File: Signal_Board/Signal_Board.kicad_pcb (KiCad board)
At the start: 2 copper layers, 54 x 43.5 mm, 17 parts, among them J1 Conn_01x02_Pin, J2 Conn_01x06_Pin, U1 74HC14, U2 LM317LZ, U3 4046

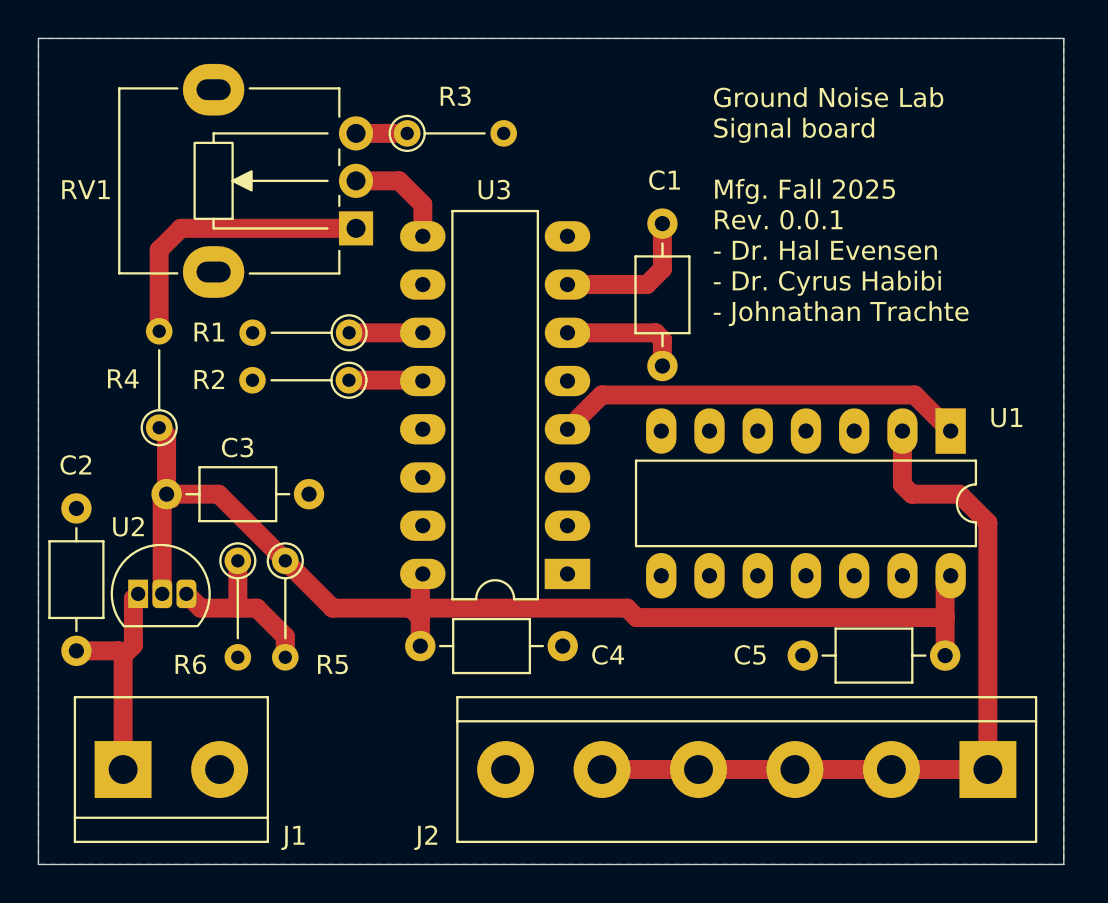
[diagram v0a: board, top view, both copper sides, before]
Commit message: Signal board version 0.0.2; updates in README
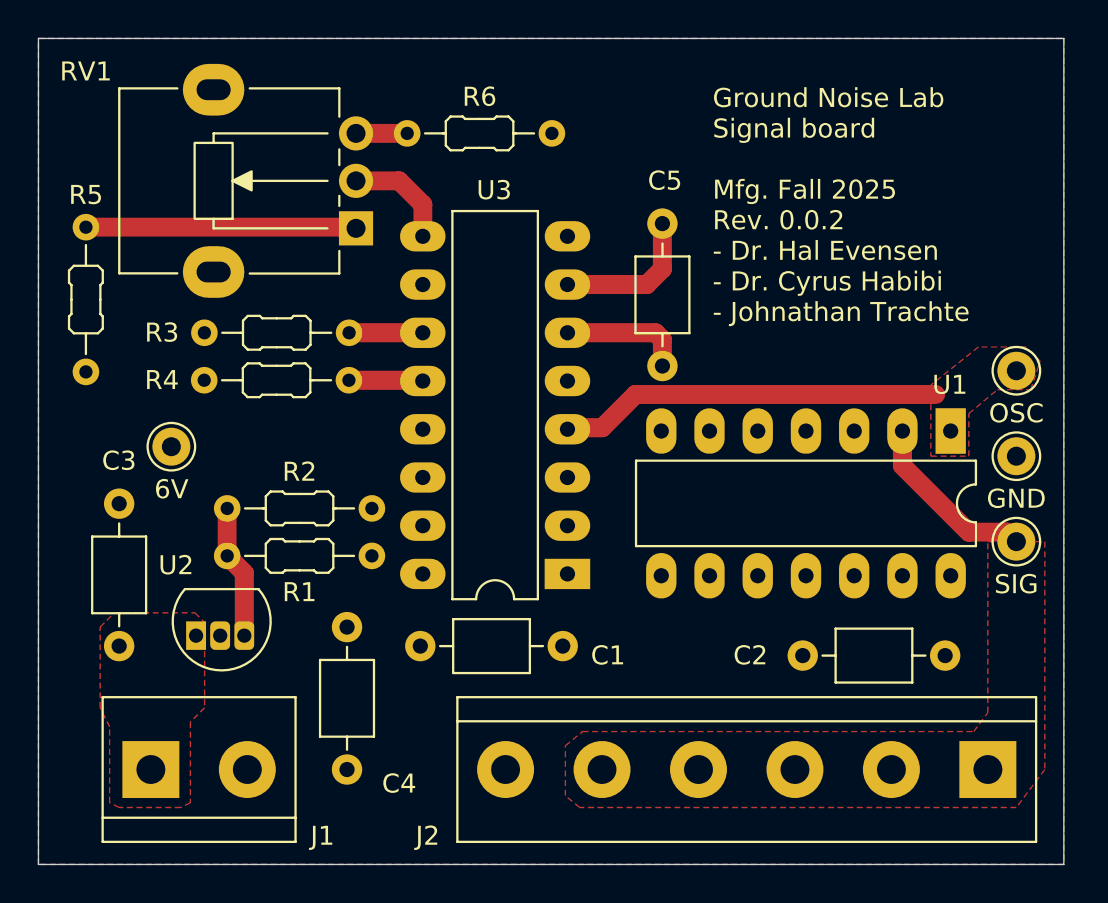
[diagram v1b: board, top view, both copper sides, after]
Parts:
- added 6V: 6 V, Connector_Pin:Pin_D1.0mm_L10.0mm, F.Cu at (115.5, 63.5)
- added GND: GND, Connector_Pin:Pin_D1.0mm_L10.0mm, F.Cu at (160.0, 64.0)
- added OSC: Osc, Connector_Pin:Pin_D1.0mm_L10.0mm, F.Cu at (160.0, 59.5)
- added SIG: Sig, Connector_Pin:Pin_D1.0mm_L10.0mm, F.Cu at (160.0, 68.5)
- R1: renamed from R5; value 1k -> 240; footprint PCM_Resistor_THT_AKL:R_Axial_DIN0204_L3.6mm_D1.6mm_P5.08mm_Vertical -> PCM_Resistor_THT_AKL:R_Axial_DIN0204_L3.6mm_D1.6mm_P7.62mm_Horizontal
- R2: renamed from R6; value 3k6 -> 910; footprint PCM_Resistor_THT_AKL:R_Axial_DIN0204_L3.6mm_D1.6mm_P5.08mm_Vertical -> PCM_Resistor_THT_AKL:R_Axial_DIN0204_L3.6mm_D1.6mm_P7.62mm_Horizontal
- R3: renamed from R1; footprint PCM_Resistor_THT_AKL:R_Axial_DIN0204_L3.6mm_D1.6mm_P5.08mm_Vertical -> PCM_Resistor_THT_AKL:R_Axial_DIN0204_L3.6mm_D1.6mm_P7.62mm_Horizontal
- R4: renamed from R2; footprint PCM_Resistor_THT_AKL:R_Axial_DIN0204_L3.6mm_D1.6mm_P5.08mm_Vertical -> PCM_Resistor_THT_AKL:R_Axial_DIN0204_L3.6mm_D1.6mm_P7.62mm_Horizontal
- R5: renamed from R4; footprint PCM_Resistor_THT_AKL:R_Axial_DIN0204_L3.6mm_D1.6mm_P5.08mm_Vertical -> PCM_Resistor_THT_AKL:R_Axial_DIN0204_L3.6mm_D1.6mm_P7.62mm_Horizontal
- R6: renamed from R3; footprint PCM_Resistor_THT_AKL:R_Axial_DIN0204_L3.6mm_D1.6mm_P5.08mm_Vertical -> PCM_Resistor_THT_AKL:R_Axial_DIN0204_L3.6mm_D1.6mm_P7.62mm_Horizontal
- moved C4 11.8 mm to (124.8, 73.0), turned to -90 degrees
- moved R5 4.85 mm to (111.0, 59.6)
- moved R1 4.57 mm to (126.1, 69.2), turned to 180 degrees
- moved U2 3.76 mm to (116.8, 73.5)
- moved R2 2.82 mm to (118.4, 66.8), turned to 0 degrees
- moved C3 2.26 mm to (112.8, 74.0)
- moved J1 1.46 mm to (114.4, 80.5)
- renumbered C4 to C1, C5 to C2, C2 to C3, C3 to C4, C1 to C5
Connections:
- U1 pad 10: GND -> unconnected-(U1-Pad10)
- U1 pad 12: GND -> unconnected-(U1-Pad12)
- U1 pad 4: GND -> unconnected-(U1-Pad4)
- U1 pad 6: GND -> unconnected-(U1-Pad6)
- U1 pad 8: GND -> unconnected-(U1-Pad8)
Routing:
- net +6V: track 61.7 -> 0.00 mm
- net /SIG_Out: track 41.5 -> 9.48 mm
- net +9V: track 12.1 -> 0.00 mm
- net /LDO_ADJ: track 9.72 -> 7.07 mm
- net OSC_Out: track 21.7 -> 20.1 mm
- net Net-(R5-Pad2): track 15.1 -> 14.2 mm
- added copper zone on F.Cu, net +6V
- added copper zone on F.Cu, net +9V
- added copper zone on F.Cu, net /SIG_Out
- added copper zone on F.Cu, net OSC_Out
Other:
- board text added: "Ground Noise Lab Signal board Mfg. Fall 2025 Rev. 0.0.2 - Dr. Hal Evensen - Dr. Cyrus Habibi - Johnathan Trachte"
- board text removed: "Ground Noise Lab Signal board Mfg. Fall 2025 Rev. 0.0.1 - Dr. Hal Evensen - Dr. Cyrus Habibi - Johnathan Trachte"
